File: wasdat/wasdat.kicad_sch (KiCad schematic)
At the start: 20 parts, among them J1 ISP, U1 ATmega32U4, U2 74HC138, X1 16mhz

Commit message: Fixing a cleaner version that is cheaper to produce.
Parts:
- removed X1: 16mhz, Keeb_components:Resonator_SMD_muRata_CSTNExxV-3Pin-p1.2, symbol keyboard_parts:XTAL_GND
- added Y2: ASCO, Oscillator:Oscillator_SMD_Abracon_ASE-4Pin_3.2x2.5mm, symbol Oscillator:ASCO
- C1, C2, C3, C4, C6: footprint Keeb_components:C_0603 -> Capacitor_SMD:C_0402_1005Metric
- C5: footprint Keeb_components:C_0805 -> Capacitor_SMD:C_0603_1608Metric
- R1, R2, R3, R4, R5, R6, R7: footprint Keeb_components:R_0603 -> Resistor_SMD:R_0402_1005Metric
- U1: footprint Keeb_components:ATMEGA32U4 -> Package_DFN_QFN:QFN-44-1EP_7x7mm_P0.5mm_EP5.15x5.15mm
- U2: footprint Package_SO:SOIC-16_3.9x9.9mm_P1.27mm -> Package_SO:TSSOP-16_4.4x5mm_P0.65mm
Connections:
- net GND: now also Y2.2 (GND)
- net VCC: now also Y2.4 (VDD)
- net at U1.17 (XTAL1): now also Y2.3 (OUT)
- no-connect marks 12 -> 14

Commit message: More clean up
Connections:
- net USB_D_M: now reaches R2.1, U1.3 (D-)
- net USB_D_P: now reaches R1.1, U1.4 (D+)
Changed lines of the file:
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@@
+		)
+	)
+	(label "USB_D_M"
+		(at 71.12 88.9 0)
+		(effects
+			(font
+				(size 1.524 1.524)
+			)
+			(justify left bottom)
+		)
+	)
+	(label "USB_D_P"
+		(at 71.12 86.36 0)
+		(effects
+			(font
+				(size 1.524 1.524)
+			)
+			(justify left bottom)
 		)
 	)

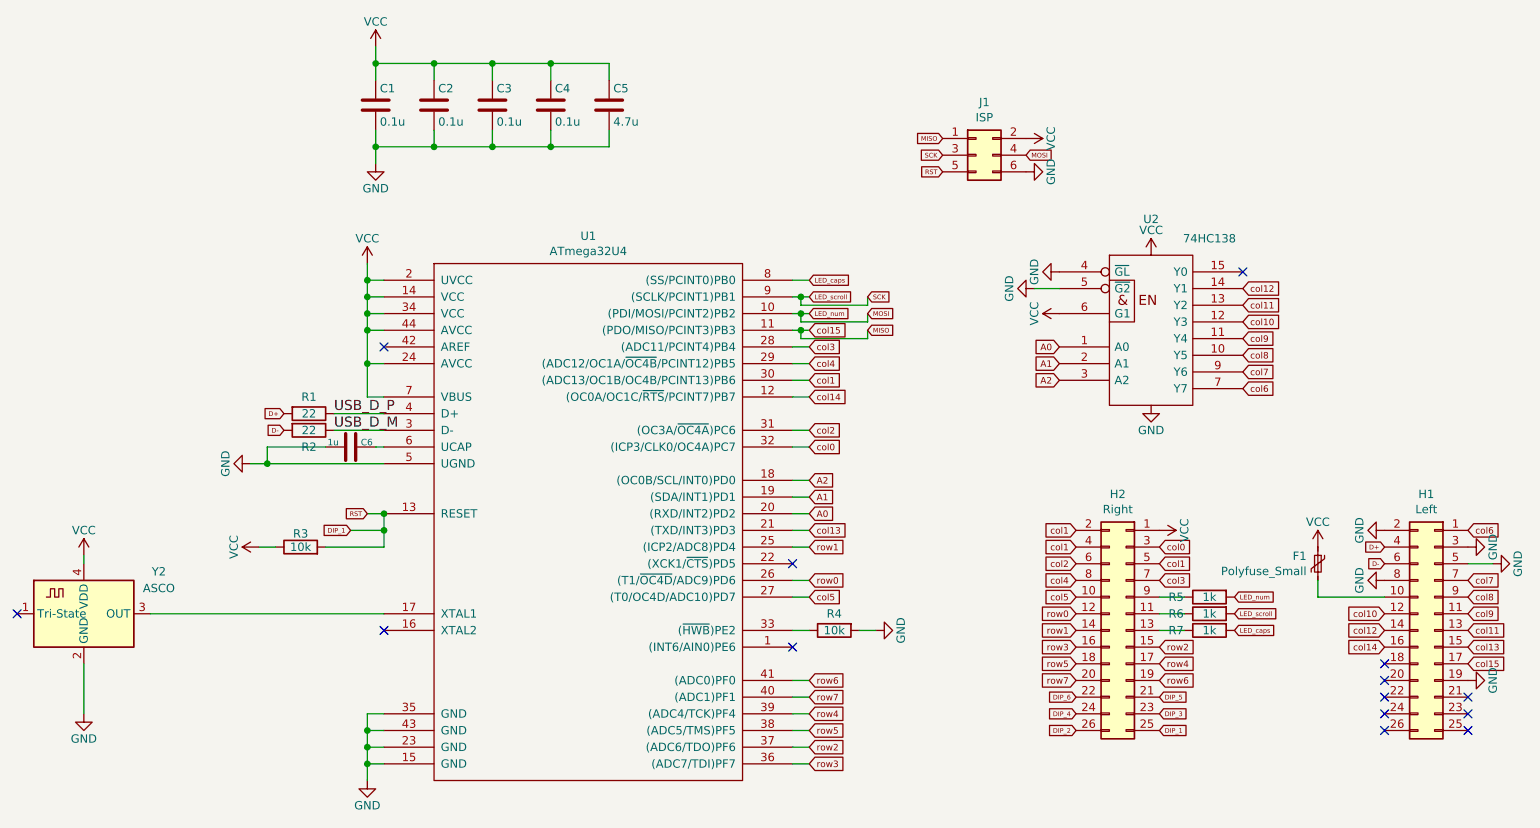
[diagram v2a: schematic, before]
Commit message: Final updates, added 2 dip sw for user usage.
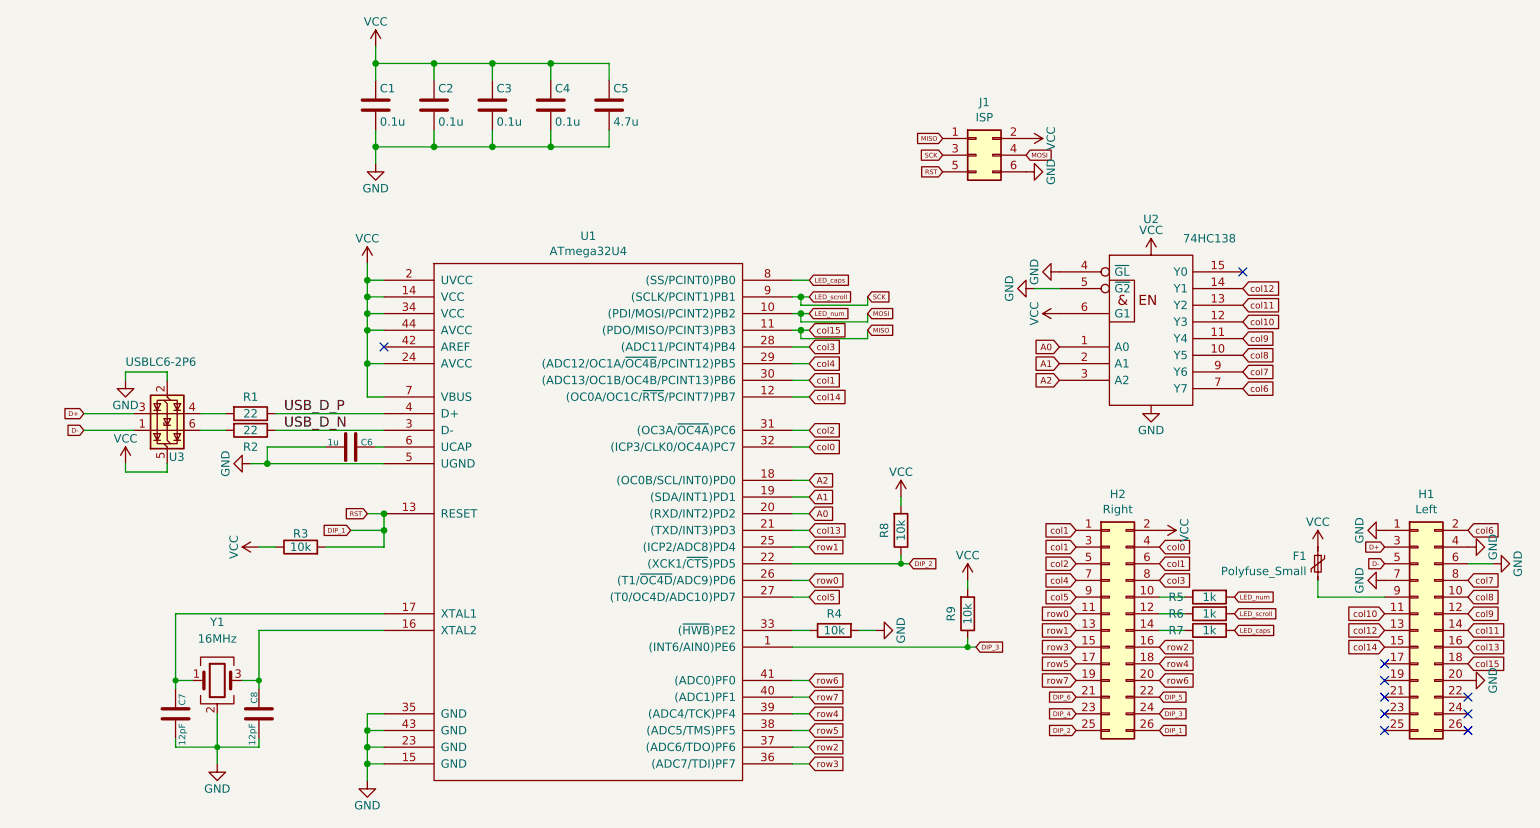
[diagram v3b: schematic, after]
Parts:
- removed Y2: ASCO, Oscillator:Oscillator_SMD_Abracon_ASE-4Pin_3.2x2.5mm, symbol Oscillator:ASCO
- added C7, C8: 12pF, Capacitor_SMD:C_0402_1005Metric, symbol Device:C
- added R8, R9: 10k, Resistor_SMD:R_0402_1005Metric, symbol Device:R
- added U3: USBLC6-2P6, Package_TO_SOT_SMD:SOT-666, symbol Power_Protection:USBLC6-2P6
- added Y1: 16MHz, Crystal:Crystal_SMD_2016-4Pin_2.0x1.6mm, symbol Device:Crystal_GND24
- C1, C2, C3, C4: LCSC (none) -> C1525
- C5: LCSC (none) -> C19666
- C6: LCSC (none) -> C52923
- F1: LCSC (none) -> C22435710
- H1, H2: LCSC (none) -> C2883299
- J1: footprint Keeb_components:isp_standard -> Connector_PinHeader_2.54mm:PinHeader_2x03_P2.54mm_Vertical
- R1, R2: LCSC (none) -> C25092
- R3, R4: LCSC (none) -> C60489
- R5, R6, R7: LCSC (none) -> C11702
- U1: LCSC (none) -> C112161
- U2: LCSC (none) -> C157527
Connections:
- net D+: now also H1.3 (Pin_3), U3.3 (I/O2); no longer H1.4 (Pin_4), R1.2
- net D-: now also H1.5 (Pin_5), U3.1 (I/O1); no longer H1.6 (Pin_6), R2.2
- net DIP_1: now also H2.26 (Pin_26); no longer H2.25 (Pin_25)
- net DIP_2: now also H2.25 (Pin_25), U1.22 ((XCK1/~{CTS})PD5), R8.1; no longer H2.26 (Pin_26)
- net DIP_3: now also H2.24 (Pin_24), U1.1 ((INT6/AIN0)PE6), R9.1; no longer H2.23 (Pin_23)
- net DIP_4: now also H2.23 (Pin_23); no longer H2.24 (Pin_24)
- net DIP_5: now also H2.22 (Pin_22); no longer H2.21 (Pin_21)
- net DIP_6: now also H2.21 (Pin_21); no longer H2.22 (Pin_22)
- net GND: now also H1.1 (Pin_1), H1.20 (Pin_20), H1.4 (Pin_4), H1.6 (Pin_6), H1.7 (Pin_7), C7.2, C8.2, U3.2 (GND), Y1.2 (G), Y1.4 (G); no longer H1.19 (Pin_19), H1.2 (Pin_2), H1.3 (Pin_3), H1.5 (Pin_5), H1.8 (Pin_8)
- net MISO: now also H1.18 (Pin_18); no longer H1.17 (Pin_17)
- net VCC: now also H2.2 (Pin_2), R8.2, R9.2, U3.5 (VBUS); no longer H2.1 (Pin_1)
- net col0: now also H2.4 (Pin_4); no longer H2.3 (Pin_3)
- net col1: now also H2.1 (Pin_1), H2.3 (Pin_3), H2.6 (Pin_6); no longer H2.2 (Pin_2), H2.4 (Pin_4), H2.5 (Pin_5)
- net col10: now also H1.11 (Pin_11); no longer H1.12 (Pin_12)
- net col11: now also H1.14 (Pin_14); no longer H1.13 (Pin_13)
- net col12: now also H1.13 (Pin_13); no longer H1.14 (Pin_14)
- net col13: now also H1.16 (Pin_16); no longer H1.15 (Pin_15)
- net col14: now also H1.15 (Pin_15); no longer H1.16 (Pin_16)
- net col2: now also H2.5 (Pin_5); no longer H2.6 (Pin_6)
- net col3: now also H2.8 (Pin_8); no longer H2.7 (Pin_7)
- net col4: now also H2.7 (Pin_7); no longer H2.8 (Pin_8)
- net col5: now also H2.9 (Pin_9); no longer H2.10 (Pin_10)
- net col6: now also H1.2 (Pin_2); no longer H1.1 (Pin_1)
- net col7: now also H1.8 (Pin_8); no longer H1.7 (Pin_7)
- net col8: now also H1.10 (Pin_10); no longer H1.9 (Pin_9)
- net col9: now also H1.12 (Pin_12); no longer H1.11 (Pin_11)
- net row0: now also H2.11 (Pin_11); no longer H2.12 (Pin_12)
- net row1: now also H2.13 (Pin_13); no longer H2.14 (Pin_14)
- net row2: now also H2.16 (Pin_16); no longer H2.15 (Pin_15)
- net row3: now also H2.15 (Pin_15); no longer H2.16 (Pin_16)
- net row4: now also H2.18 (Pin_18); no longer H2.17 (Pin_17)
- net row5: now also H2.17 (Pin_17); no longer H2.18 (Pin_18)
- net row6: now also H2.20 (Pin_20); no longer H2.19 (Pin_19)
- net row7: now also H2.19 (Pin_19); no longer H2.20 (Pin_20)
- net at U1.16 (XTAL2): now also C8.1, Y1.3
- net at U1.17 (XTAL1): now also C7.1, Y1.1
- net at F1.2: now also H1.9 (Pin_9); no longer H1.10 (Pin_10)
- net at R6.1: now also H2.12 (Pin_12); no longer H2.11 (Pin_11)
- net at R7.1: now also H2.14 (Pin_14); no longer H2.13 (Pin_13)
- net at R5.1: now also H2.10 (Pin_10); no longer H2.9 (Pin_9)
- net USB_D_M renamed USB_D_N
- new net: R1.2, U3.4 (I/O2)
- new net: R2.2, U3.6 (I/O1)
- no-connect marks 14 -> 10
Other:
- moved on the sheet: R1, R2
